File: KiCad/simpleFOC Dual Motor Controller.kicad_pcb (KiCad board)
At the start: 2 copper layers, 50 x 50 mm, 27 parts, among them Q301 MS6001Y, Q302 MS6001Y, Q401 MS6001Y, Q402 MS6001Y, Q501 MS6001Y, Q502 MS6001Y, Q701 MS6001Y, Q702 MS6001Y, Q801 MS6001Y, Q802 MS6001Y, Q901 MS6001Y, Q902 MS6001Y, U101 STM32F103C8Tx, U201 DRV8323HRTAT, U601 DRV8323HRTAT

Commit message: added board design rules
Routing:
- added copper zone on In1.Cu, net /Motor Driver 1/Motor_VIN
- added copper zone on In2.Cu, net GND
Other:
- copper layers 2 -> 4

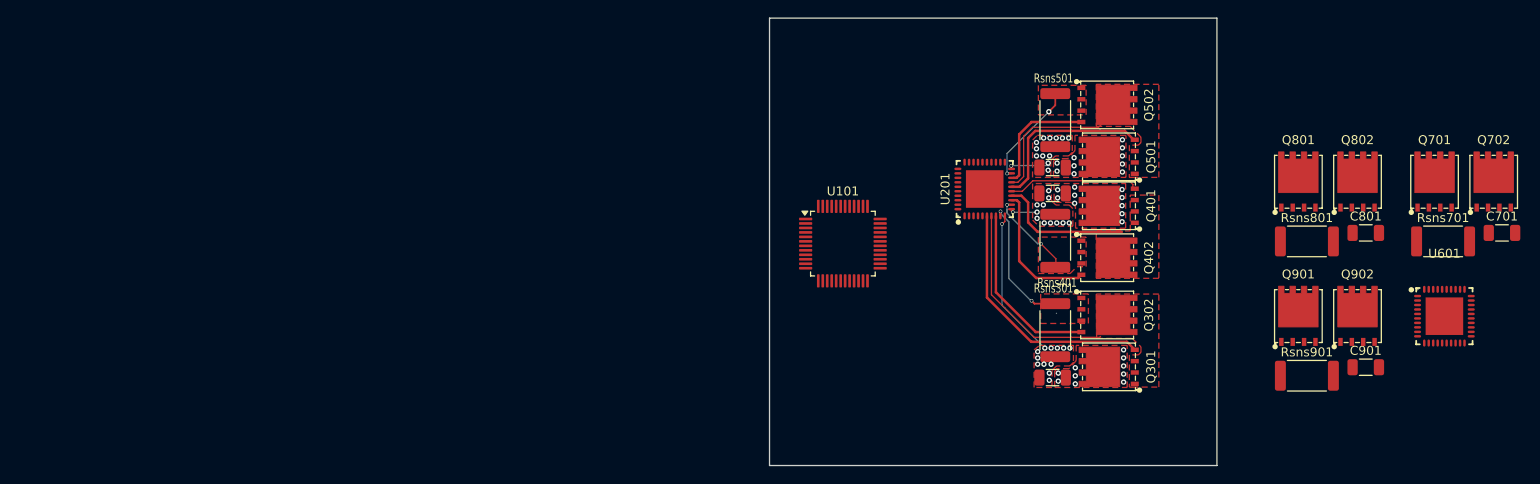
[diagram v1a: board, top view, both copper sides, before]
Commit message: Finished wiring motor drive circuitry
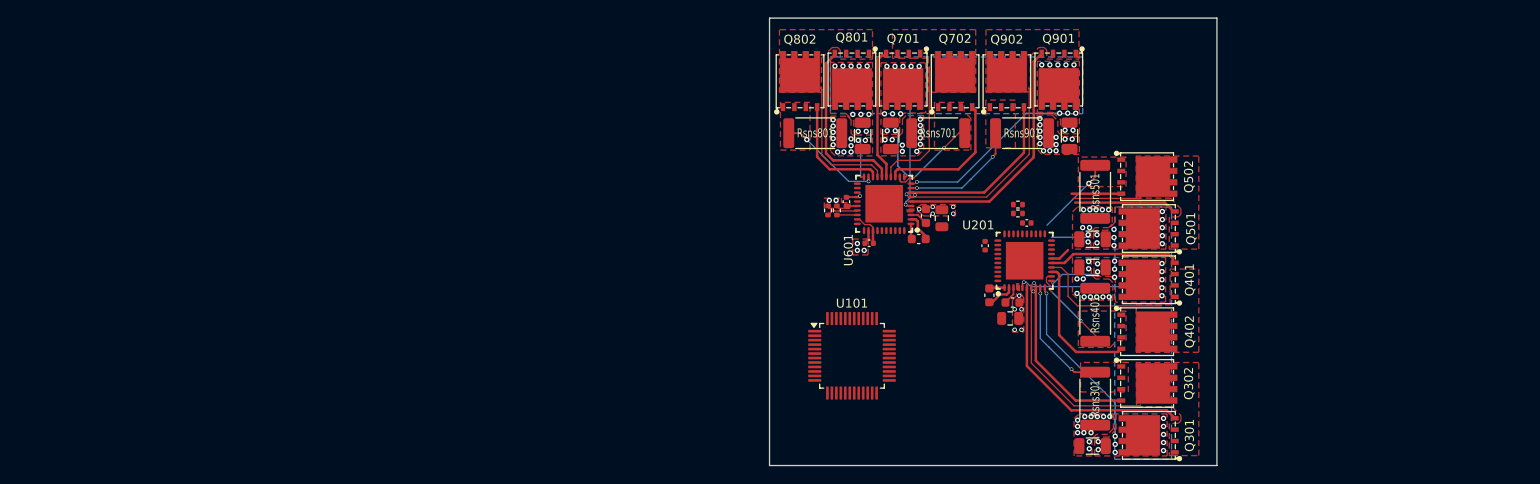
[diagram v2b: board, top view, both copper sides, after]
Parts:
- added C201: 100n, Capacitor_SMD:C_0805_2012Metric, F.Cu at (126.9, 58.6)
- added C202: 1u, Capacitor_SMD:C_0603_1608Metric, F.Cu at (127.1, 56.8)
- added C203: 47n, Capacitor_SMD:C_0603_1608Metric, F.Cu at (124.6, 56.0)
- added C204: 1u, Capacitor_SMD:C_0402_1005Metric, F.Cu at (124.1, 50.4)
- added C205: 0.1u, Capacitor_SMD:C_0402_1005Metric, F.Cu at (128.8, 47.9)
- added C601: 100n, Capacitor_SMD:C_0805_2012Metric, F.Cu at (119.3, 47.4)
- added C602: 1u, Capacitor_SMD:C_0603_1608Metric, F.Cu at (117.5, 47.1)
- added C603: 47n, Capacitor_SMD:C_0603_1608Metric, F.Cu at (116.7, 49.7)
- added C604: 1u, Capacitor_SMD:C_0402_1005Metric, F.Cu at (111.1, 50.2)
- added C605: 0.1u, Capacitor_SMD:C_0402_1005Metric, F.Cu at (108.6, 45.5)
- added R201: 75k, Resistor_SMD:R_0402_1005Metric, F.Cu at (127.8, 45.8)
- added R202: 75k, Resistor_SMD:R_0402_1005Metric, F.Cu at (127.8, 46.8)
- added R601: 75k, Resistor_SMD:R_0402_1005Metric, F.Cu at (106.5, 46.5)
- added R602: 75k, Resistor_SMD:R_0402_1005Metric, F.Cu at (107.5, 46.5)
- moved U601 63.9 mm to (112.8, 45.7), turned to 180 degrees
- moved Q802 63.3 mm to (103.4, 33.2)
- moved C901 61.9 mm to (110.4, 38.2), turned to -90 degrees
- moved Q702 61.2 mm to (120.7, 33.2)
- moved Q701 60.9 mm to (114.9, 30.8), turned to 180 degrees
- moved Rsns701 57.7 mm to (118.9, 37.9), turned to 180 degrees
- moved Rsns801 56.3 mm to (105.1, 37.9)
- moved C801 54.2 mm to (113.6, 38.2), turned to -90 degrees
- moved Q801 51.7 mm to (109.2, 30.8), turned to 180 degrees
- moved C701 49.5 mm to (133.5, 38.2), turned to -90 degrees
- moved Q902 47.2 mm to (126.5, 33.2)
- moved Rsns901 41.8 mm to (128.2, 37.9)
- moved Q901 39.2 mm to (132.3, 30.8), turned to 180 degrees
- moved U101 12.6 mm to (109.2, 62.7)
- moved C401 9.40 mm to (136.1, 52.9)
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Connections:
- U201 pad 1: unconnected-(U201-CPL-Pad1) -> Net-(U201-CPL)
- U201 pad 2: unconnected-(U201-CPH-Pad2) -> Net-(U201-CPH)
- U201 pad 24: unconnected-(U201-VREF-Pad24) -> /Motor Driver 1/VREF
- U201 pad 26: unconnected-(U201-MODE-Pad26) -> GND
- U201 pad 27: unconnected-(U201-IDRIVE-Pad27) -> Net-(U201-IDRIVE)
- U201 pad 28: unconnected-(U201-VDS-Pad28) -> Net-(U201-VDS)
- U201 pad 29: unconnected-(U201-GAIN-Pad29) -> /Motor Driver 1/DVDD
- U201 pad 32: unconnected-(U201-AGND-Pad32) -> GND
- U201 pad 33: unconnected-(U201-DVDD-Pad33) -> /Motor Driver 1/DVDD
- U201 pad 40: unconnected-(U201-PGND-Pad40) -> GND
- U201 pad 41: unconnected-(U201-EP-Pad41) -> GND
- U601 pad 1: unconnected-(U601-CPL-Pad1) -> Net-(U601-CPL)
- U601 pad 2: unconnected-(U601-CPH-Pad2) -> Net-(U601-CPH)
- U601 pad 24: unconnected-(U601-VREF-Pad24) -> /Motor Driver 2/VREF
- U601 pad 26: unconnected-(U601-MODE-Pad26) -> GND
- U601 pad 27: unconnected-(U601-IDRIVE-Pad27) -> Net-(U601-IDRIVE)
- U601 pad 28: unconnected-(U601-VDS-Pad28) -> Net-(U601-VDS)
- U601 pad 29: unconnected-(U601-GAIN-Pad29) -> /Motor Driver 2/DVDD
- U601 pad 32: unconnected-(U601-AGND-Pad32) -> GND
- U601 pad 33: unconnected-(U601-DVDD-Pad33) -> /Motor Driver 2/DVDD
- U601 pad 40: unconnected-(U601-PGND-Pad40) -> GND
- U601 pad 41: unconnected-(U601-EP-Pad41) -> GND
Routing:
- net GND: track 26.0 -> 53.8 mm, vias 38 -> 74
- net /Motor Driver 2/Pole 1/GH: track 0.00 -> 27.7 mm
- net /Motor Driver 2/Pole 1/PoleOut: track 0.00 -> 22.7 mm
- net /Motor Driver 2/Motor_VIN: track 0.00 -> 20.2 mm, vias 0 -> 36
- net /Motor Driver 1/Motor_VIN: track 0.00 -> 20.2 mm, vias 30 -> 36
- net /Motor Driver 2/Pole 1/GL: track 0.00 -> 19.8 mm
- net /Motor Driver 2/Pole 3/GH: track 0.00 -> 19.3 mm
- net /Motor Driver 2/Pole 3/PoleOut: track 0.00 -> 18.1 mm
- net /Motor Driver 2/Pole 2/GL: track 0.00 -> 15.6 mm
- net /Motor Driver 2/Pole 2/PoleOut: track 0.00 -> 15.6 mm
- net /Motor Driver 2/Pole 2/GH: track 0.00 -> 14.8 mm
- net /Motor Driver 2/Pole 1/SP: track 0.00 -> 13.6 mm, vias 0 -> 2
- net /Motor Driver 2/Pole 3/GL: track 0.00 -> 12.9 mm
- net /Motor Driver 2/Pole 3/SP: track 0.00 -> 11.7 mm, vias 0 -> 2
- net /Motor Driver 2/Pole 2/SP: track 0.00 -> 10.0 mm, vias 0 -> 2
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- added copper zone on B.Cu, net /Motor Driver 1/Motor_VIN
- added copper zone on In2.Cu, net /Motor Driver 1/Motor_VIN
- added copper zone on B.Cu, net /Motor Driver 2/Motor_VIN
- added copper zone on F.Cu, net /Motor Driver 2/Motor_VIN
- added copper zone on F.Cu, net /Motor Driver 2/Pole 1/PoleOut
- added copper zone on F.Cu, net /Motor Driver 2/Pole 1/SP
- added copper zone on F.Cu, net /Motor Driver 2/Pole 2/PoleOut
- added copper zone on F.Cu, net /Motor Driver 2/Pole 2/SP
- added copper zone on F.Cu, net /Motor Driver 2/Pole 3/PoleOut
- added copper zone on F.Cu, net /Motor Driver 2/Pole 3/SP
- added copper zone on In1.Cu, net GND
- removed copper zone on In1.Cu, net /Motor Driver 1/Motor_VIN
- removed copper zone on In2.Cu, net GND

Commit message: started adding supporting components
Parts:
- added CN101: MR60-F, easyeda2kicad:CONN-TH_3P-P5.50_MR60-F, F.Cu at (122.9, 69.1)
- added D101: SMAJ36A, Diode_SMD:D_SMA, F.Cu at (124.5, 62.0)
- added D103: DSK26_C7502712, easyeda2kicad:SOD-123FL_L2.7-W1.8-LS3.8-RD, F.Cu at (118.1, 59.7)
- added D104: SMF5.0A_C19077497, easyeda2kicad:SOD-123FL_L2.7-W1.8-LS3.8-RD, F.Cu at (118.1, 62.2)
- added H101: MountingHole, MountingHole:MountingHole_4.3mm_M4, F.Cu at (142.8, 32.3)
- added H102: MountingHole, MountingHole:MountingHole_4.3mm_M4, F.Cu at (104.6, 70.4)
- moved U101 4.79 mm to (106.7, 58.7), turned to -90 degrees
- moved Q502 0.33 mm to (141.3, 43.0)
- moved Rsns401 0.33 mm to (136.6, 58.4)
- moved U201 0.33 mm to (128.7, 52.4)
- moved C201 0.33 mm to (127.1, 58.8)
- moved C205 0.33 mm to (129.0, 48.1)
- moved Q402 0.33 mm to (141.3, 60.3)
- moved Rsns501 0.33 mm to (136.6, 44.7)
- moved C202 0.33 mm to (127.4, 57.0)
- moved Q302 0.33 mm to (141.3, 66.1)
- moved Rsns301 0.33 mm to (136.6, 67.8)
- moved C203 0.33 mm to (124.8, 56.2)
- moved C204 0.33 mm to (124.3, 50.7)
- moved R201 0.33 mm to (128.0, 46.1)
- moved R202 0.33 mm to (128.0, 47.1)
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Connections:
- C601 pad 1: /Motor Driver 2/Motor_VIN -> /Motor Driver 1/Motor_VIN
- C602 pad 1: /Motor Driver 2/Motor_VIN -> /Motor Driver 1/Motor_VIN
- C701 pad 1: /Motor Driver 2/Motor_VIN -> /Motor Driver 1/Motor_VIN
- C801 pad 1: /Motor Driver 2/Motor_VIN -> /Motor Driver 1/Motor_VIN
- C901 pad 1: /Motor Driver 2/Motor_VIN -> /Motor Driver 1/Motor_VIN
- Q701 pad 5: /Motor Driver 2/Motor_VIN -> /Motor Driver 1/Motor_VIN
- Q801 pad 5: /Motor Driver 2/Motor_VIN -> /Motor Driver 1/Motor_VIN
- Q901 pad 5: /Motor Driver 2/Motor_VIN -> /Motor Driver 1/Motor_VIN
- U101 pad 1: unconnected-(U101-VBAT-Pad1) -> +3.3V
- U101 pad 23: Net-(U101-VSS-Pad23) -> GND
- U101 pad 24: unconnected-(U101-VDD-Pad24) -> +3.3V
- U101 pad 35: Net-(U101-VSS-Pad23) -> GND
- U101 pad 36: unconnected-(U101-VDD-Pad36) -> +3.3V
- U101 pad 47: Net-(U101-VSS-Pad23) -> GND
- U101 pad 48: unconnected-(U101-VDD-Pad48) -> +3.3V
- U101 pad 8: unconnected-(U101-VSSA-Pad8) -> GND
- U101 pad 9: unconnected-(U101-VDDA-Pad9) -> +3.3V
- U601 pad 4: /Motor Driver 2/Motor_VIN -> /Motor Driver 1/Motor_VIN
- U601 pad 5: /Motor Driver 2/Motor_VIN -> /Motor Driver 1/Motor_VIN
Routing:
- net GND: track 53.8 -> 139.6 mm, vias 74 -> 117
- net /Motor Driver 2/Motor_VIN: track 20.2 -> 0.00 mm, vias 36 -> 0
- net /Motor Driver 1/Motor_VIN: track 20.2 -> 36.9 mm, vias 36 -> 71
- net Net-(D103-A): track 0.00 -> 11.6 mm
- net /Motor Driver 1/Pole 3/GL: track 5.63 -> 12.9 mm
- net /Motor Driver 1/Pole 3/PoleOut: track 10.5 -> 17.3 mm
- net /Motor Driver 1/Pole 3/GH: track 13.6 -> 19.3 mm
- net /Motor Driver 1/DVDD: track 0.00 -> 3.61 mm
- net Net-(U201-IDRIVE): track 0.00 -> 3.40 mm
- net /Motor Driver 1/Pole 3/SP: track 8.92 -> 11.7 mm, vias 1 -> 2
- net Net-(U201-VDS): track 0.00 -> 2.44 mm
- net /Motor Driver 1/VREF: track 0.00 -> 0.98 mm, vias 0 -> 1
- net /Motor Driver 2/Pole 3/PoleOut: track 18.1 -> 17.3 mm
- removed copper zone on B.Cu, net /Motor Driver 2/Motor_VIN
- removed copper zone on F.Cu, net /Motor Driver 2/Motor_VIN

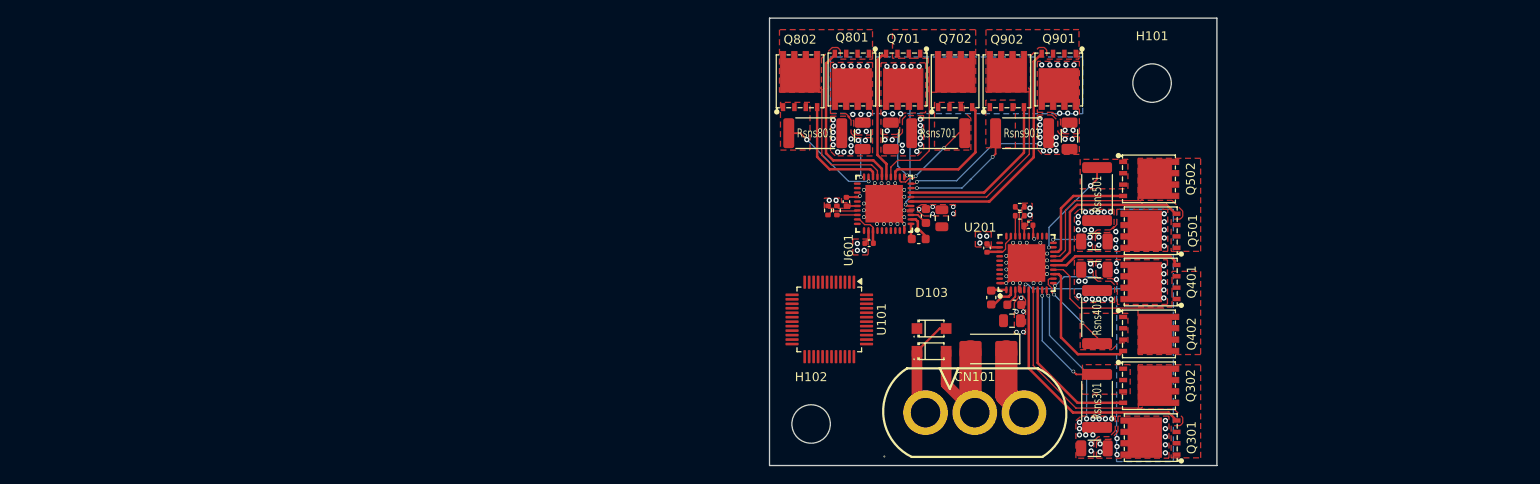
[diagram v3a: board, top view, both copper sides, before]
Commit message: rewired the board with smaller mosfets
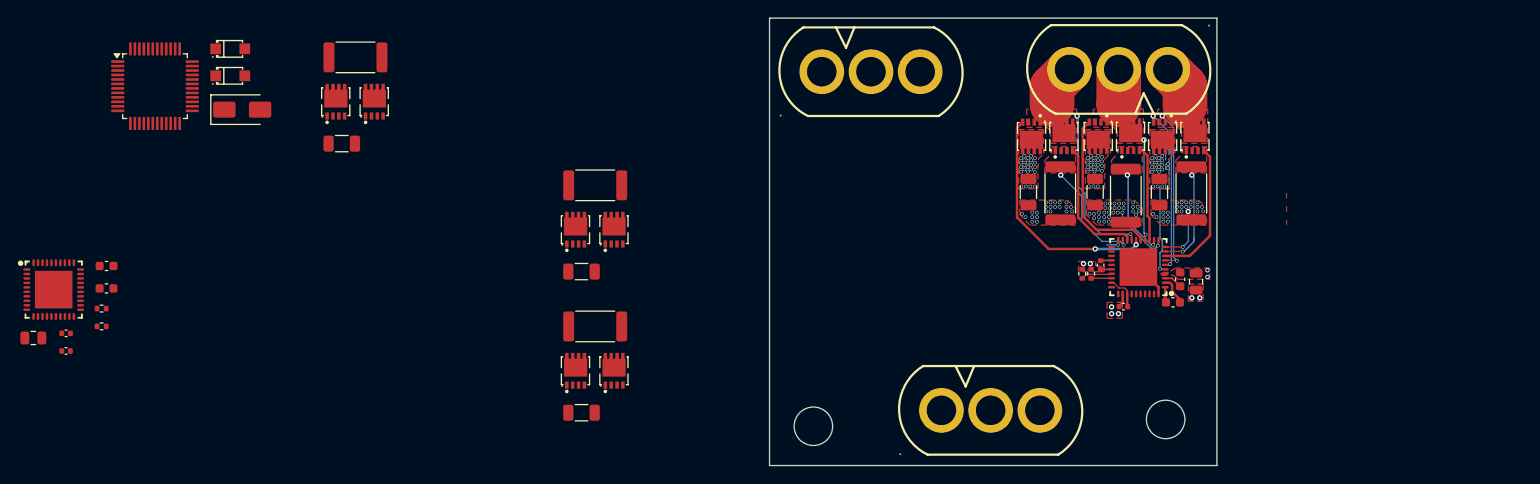
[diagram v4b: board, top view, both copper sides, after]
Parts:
- removed Q302, Q402, Q502, Q702, Q802, Q902: MS6001Y, easyeda2kicad:TDSON-8_L5.9-W5.2-P1.27-BL
- added CN201: MR60-F, easyeda2kicad:CONN-TH_3P-P5.50_MR60-F, F.Cu at (139.0, 30.7)
- added CN601: MR60-F, easyeda2kicad:CONN-TH_3P-P5.50_MR60-F, F.Cu at (111.3, 31.0)
- added NT201: NetTie_2, CustomNetTie:NetTie0.127mm, B.Cu at (146.8, 47.5)
- added NT202: NetTie_2, CustomNetTie:NetTie0.127mm, B.Cu at (139.4, 47.1)
- added NT203: NetTie_2, CustomNetTie:NetTie0.127mm, B.Cu at (137.9, 50.3)
- added NT601: NetTie_2, CustomNetTie:NetTie0.127mm, F.Cu at (157.8, 44.8)
- added NT602: NetTie_2, CustomNetTie:NetTie0.127mm, F.Cu at (157.8, 46.3)
- added NT603: NetTie_2, CustomNetTie:NetTie0.127mm, F.Cu at (157.8, 47.8)
- added Q303: AGM6014AP, easyeda2kicad:PDFN-8_L3.1-W3.0-P0.65-LS3.3-BL, F.Cu at (147.6, 38.2)
- added Q403: AGM6014AP, easyeda2kicad:PDFN-8_L3.1-W3.0-P0.65-LS3.3-BL, F.Cu at (140.4, 38.2)
- added Q503: AGM6014AP, easyeda2kicad:PDFN-8_L3.1-W3.0-P0.65-LS3.3-BL, F.Cu at (132.9, 38.2)
- added Q703: AGM6014AP, easyeda2kicad:PDFN-8_L3.1-W3.0-P0.65-LS3.3-BL, F.Cu at (55.8, 34.3)
- added Q803: AGM6014AP, easyeda2kicad:PDFN-8_L3.1-W3.0-P0.65-LS3.3-BL, F.Cu at (82.6, 48.6)
- added Q903: AGM6014AP, easyeda2kicad:PDFN-8_L3.1-W3.0-P0.65-LS3.3-BL, F.Cu at (82.6, 64.4)
- Q301, Q401, Q501, Q701, Q801, Q901: value MS6001Y -> AGM6014AP; footprint easyeda2kicad:TDSON-8_L5.9-W5.2-P1.27-BL -> easyeda2kicad:PDFN-8_L3.1-W3.0-P0.65-LS3.3-BL
- moved C601 102.4 mm to (17.7, 60.7), turned to 0 degrees
- moved U601 93.3 mm to (20.0, 55.3), turned to 0 degrees
- moved C602 91.7 mm to (25.9, 52.7), turned to 0 degrees
- moved C603 90.9 mm to (25.9, 55.2)
- moved C604 90.3 mm to (21.4, 60.2), turned to 0 degrees
- moved C605 88.8 mm to (21.4, 62.2), turned to 0 degrees
- moved D101 87.6 mm to (41.1, 35.2), turned to 0 degrees
- moved D103 84.4 mm to (39.7, 28.4)
- moved D104 84.2 mm to (39.7, 31.4)
- moved R602 83.2 mm to (25.4, 59.4), turned to 0 degrees
- moved R601 81.9 mm to (25.4, 57.5), turned to 0 degrees
- moved C701 81.3 mm to (52.2, 39.0), turned to 0 degrees
- moved U101 79.7 mm to (31.3, 32.6), turned to 0 degrees
- moved Rsns701 65.7 mm to (53.7, 29.4), turned to 0 degrees
- moved Q901 63.6 mm to (78.3, 64.4), turned to 0 degrees
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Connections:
- C204 pad 2: GND -> /Motor Driver 1/Motor_VIN
- C205 pad 2: GND -> /Motor Driver 1/Motor_VIN
- Rsns301 pad 2: GND -> /Motor Driver 1/Motor_VIN
- U201 pad 10: GND -> Net-(U201-SNA)
- U201 pad 11: GND -> Net-(U201-SNB)
- U201 pad 20: GND -> Net-(U201-SNC)
- U201 pad 26: GND -> /Motor Driver 1/Motor_VIN
- U201 pad 32: GND -> /Motor Driver 1/Motor_VIN
- U601 pad 10: GND -> Net-(U601-SNA)
- U601 pad 11: GND -> Net-(U601-SNB)
- U601 pad 20: GND -> Net-(U601-SNC)
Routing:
- net GND: track 139.6 -> 3.93 mm, vias 117 -> 86
- net /Motor Driver 2/Pole 1/GH: track 27.7 -> 0.00 mm
- net /Motor Driver 2/Pole 1/PoleOut: track 22.7 -> 0.00 mm
- net /Motor Driver 1/Motor_VIN: track 36.9 -> 14.7 mm, vias 71 -> 70
- net /Motor Driver 2/Pole 1/GL: track 19.8 -> 0.00 mm
- net /Motor Driver 2/Pole 3/GH: track 19.3 -> 0.00 mm
- net /Motor Driver 2/Pole 3/PoleOut: track 17.3 -> 0.00 mm
- net /Motor Driver 2/Pole 2/GL: track 15.6 -> 0.00 mm
- net /Motor Driver 2/Pole 2/PoleOut: track 15.6 -> 0.00 mm
- net /Motor Driver 2/Pole 2/GH: track 14.8 -> 0.00 mm
- net /Motor Driver 2/Pole 1/SP: track 13.6 -> 0.00 mm, vias 2 -> 0
- net /Motor Driver 2/Pole 3/GL: track 12.9 -> 0.00 mm
- net /Motor Driver 2/Pole 3/SP: track 11.7 -> 0.00 mm, vias 2 -> 0
- net Net-(D103-A): track 11.6 -> 0.00 mm
- net /Motor Driver 2/Pole 2/SP: track 10.0 -> 0.00 mm, vias 2 -> 0
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- added copper zone on B.Cu, net GND
- removed copper zone on B.Cu, net /Motor Driver 1/Motor_VIN
- removed copper zone on F.Cu, net /Motor Driver 2/Pole 1/PoleOut
- removed copper zone on F.Cu, net /Motor Driver 2/Pole 1/SP
- removed copper zone on F.Cu, net /Motor Driver 2/Pole 2/PoleOut
- removed copper zone on F.Cu, net /Motor Driver 2/Pole 2/SP
- removed copper zone on F.Cu, net /Motor Driver 2/Pole 3/PoleOut
- removed copper zone on F.Cu, net /Motor Driver 2/Pole 3/SP
